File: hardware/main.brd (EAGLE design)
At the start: 91.5 x 58.5 mm, 40 parts, among them U1 TMS320F28069_PN_80, U10 TXB0101_DBV_6, U2 TXB0101_DBV_6, U3 TS3A5018_PW_16, U4 TS3A5018_PW_16, U5 SN74LVC4245A_DW_24, U7 Value, U8 Value, U9 SN74LVC4245A_DW_24

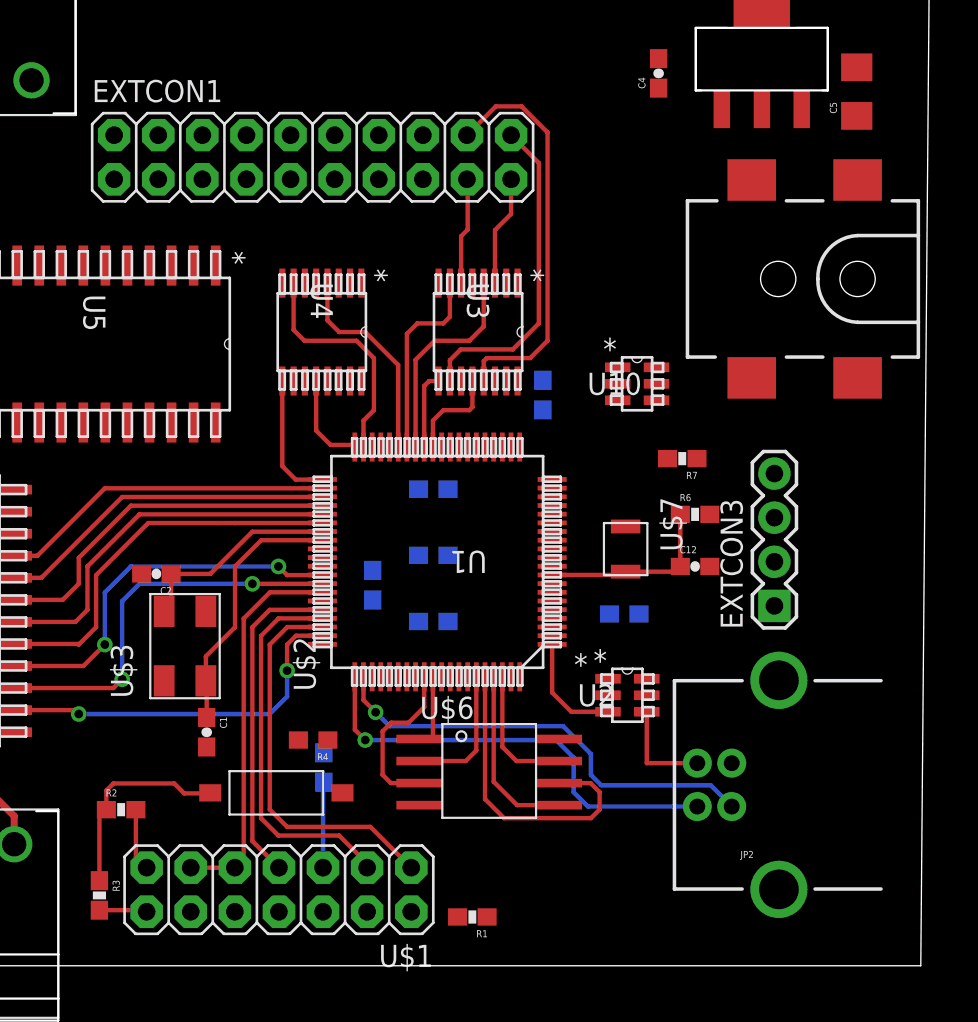
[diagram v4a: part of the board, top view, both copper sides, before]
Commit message: Ripped up USB routing, SPI routing, and previously made input stage routing. Starting over.
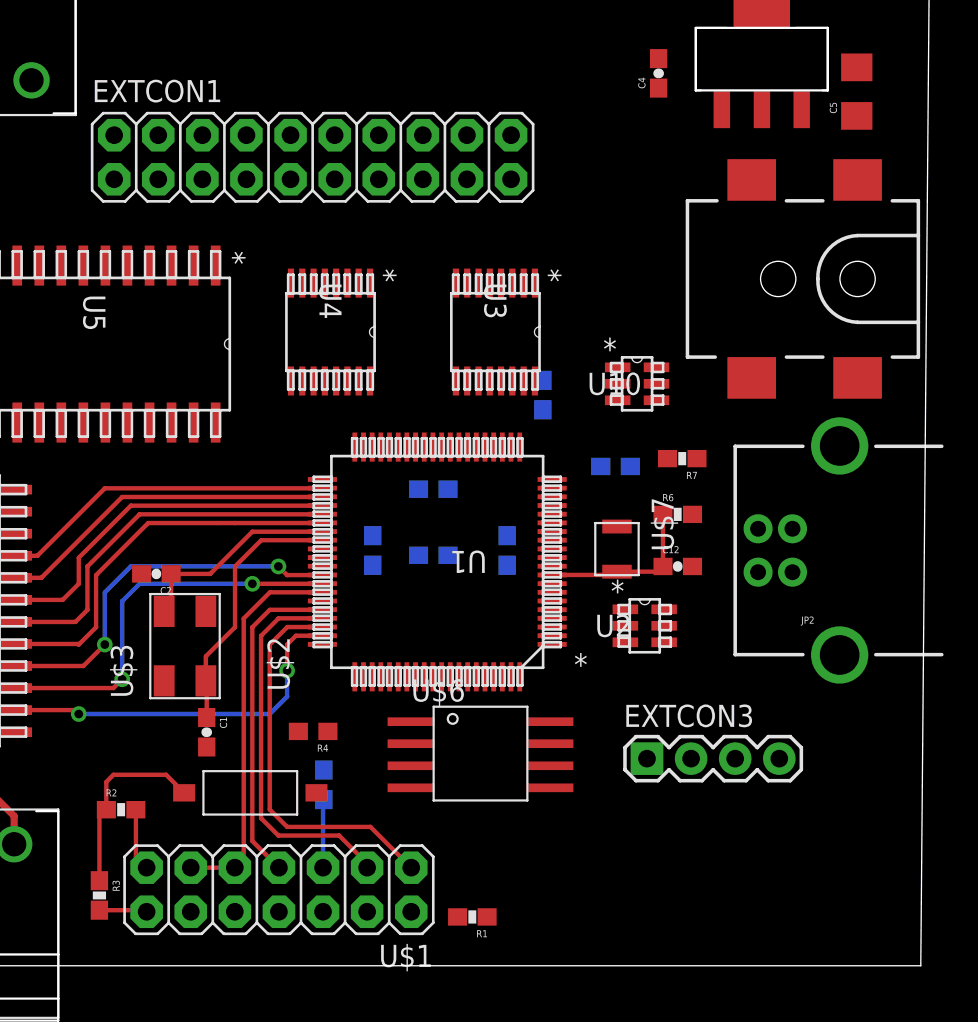
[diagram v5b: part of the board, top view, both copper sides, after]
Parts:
- moved JP2 13.9 mm to (83.6, 23.9)
- moved EXTCON3 11.5 mm to (75.2, 11.9), turned to 0 degrees
- moved C8 8.51 mm to (73.4, 28.8)
- moved C11 5.90 mm to (67.2, 23.9), turned to 270 degrees
- moved U2 4.12 mm to (75.1, 19.6)
- moved C7 2.00 mm to (59.4, 23.9)
- moved U$2 1.50 mm to (52.4, 9.96)
- moved U$6 1.12 mm to (65.6, 12.2)
- moved C12 1.00 mm to (77.0, 23.0)
- moved C6 1.00 mm to (56.6, 10.4)
- moved R6 1.00 mm to (77.0, 26.0)
- moved U3 1.00 mm to (66.5, 36.5)
- moved R4 0.50 mm to (56.0, 13.5)
- moved U$7 0.50 mm to (73.5, 24.0)
- moved U4 0.50 mm to (57.0, 36.5)
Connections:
- net USBDM renamed USB_N
- net USBDP renamed USB_P
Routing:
- net USB_P: track 25.8 -> 0.00 mm, vias 1 -> 0
- net USB_N: track 25.8 -> 0.00 mm, vias 1 -> 0
- net SW4: track 23.3 -> 0.00 mm
- net SW3: track 18.7 -> 0.00 mm
- net SPICLK: track 17.9 -> 0.00 mm
- net UCIN6: track 13.4 -> 0.00 mm
- net UCIN1: track 12.2 -> 0.00 mm
- net UCIN5: track 12.0 -> 0.00 mm
- net UCIN2: track 11.3 -> 0.00 mm
- net SPISIMO: track 10.3 -> 0.00 mm
- net !FLASHWP!: track 9.56 -> 0.00 mm
- net SPISOMI: track 7.76 -> 0.00 mm
- net !FLASHHOLD!: track 7.62 -> 0.00 mm
- net UCIN7: track 7.54 -> 0.00 mm
- net USBMON: track 6.63 -> 0.00 mm
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
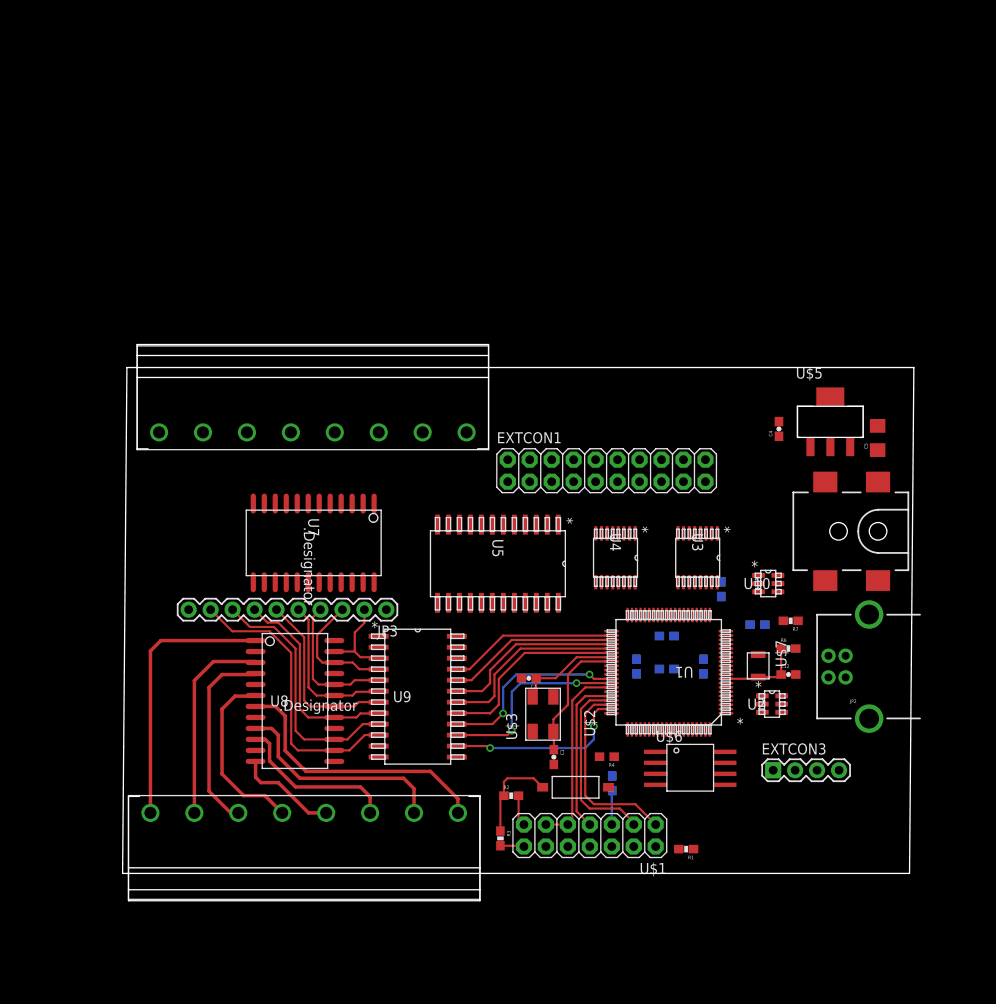
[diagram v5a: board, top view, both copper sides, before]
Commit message: Beginning new layout and routing. Clock traces and USB routed first.
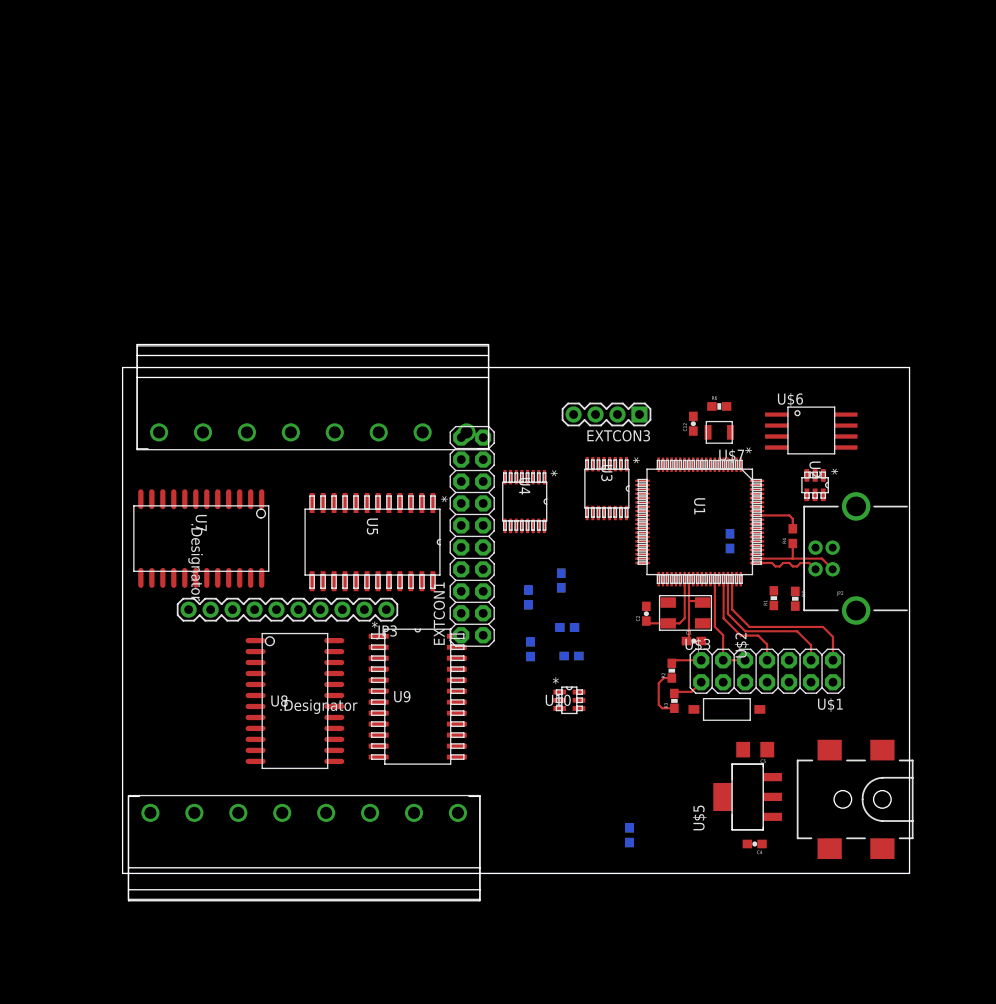
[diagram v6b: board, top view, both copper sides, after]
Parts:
- moved C4 48.1 mm to (73.1, 3.40), turned to 180 degrees
- moved U$5 44.4 mm to (72.3, 8.84), turned to 90 degrees
- moved EXTCON3 43.9 mm to (59.8, 53.1), turned to 180 degrees
- moved U$6 41.4 mm to (79.6, 51.2)
- moved C5 38.7 mm to (73.2, 14.3), turned to 180 degrees
- moved R4 33.4 mm to (77.5, 39.0), turned to 90 degrees
- moved C12 31.0 mm to (66.0, 52.0), turned to 90 degrees
- moved JP1 31.0 mm to (87.9, 8.56)
- moved R1 30.7 mm to (75.3, 31.8), turned to 90 degrees
- moved R6 29.1 mm to (69.0, 54.0)
- moved U$1 28.0 mm to (82.2, 24.6)
- moved U$7 27.4 mm to (69.0, 51.0), turned to 180 degrees
- moved U10 26.7 mm to (51.7, 20.0)
- moved U2 25.8 mm to (80.1, 44.9), turned to 270 degrees
- moved R3 25.6 mm to (63.8, 19.9), turned to 90 degrees
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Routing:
- net N$9: track 33.1 -> 0.00 mm
- net N$20: track 31.8 -> 0.00 mm
- net N$13: track 31.4 -> 0.00 mm
- net N$10: track 29.4 -> 0.00 mm
- net N$19: track 25.5 -> 0.00 mm
- net N$11: track 24.1 -> 0.00 mm
- net N$14: track 23.4 -> 0.00 mm
- net UCOUT7: track 23.0 -> 0.00 mm, vias 2 -> 0
- net UCOUT5: track 22.6 -> 0.00 mm
- net N$15: track 22.5 -> 0.00 mm
- net UCOUT6: track 22.2 -> 0.00 mm, vias 2 -> 0
- net UCOUT4: track 21.9 -> 0.00 mm
- net UCOUT8: track 21.6 -> 0.00 mm, vias 2 -> 0
- net UCOUT3: track 21.0 -> 0.00 mm
- net N$12: track 20.9 -> 0.00 mm
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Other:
- board size 91.5 x 58.5 mm -> 91 x 58.5 mm

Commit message: Change analog switch for input selection to buffer. Reviewed and reworked enable pin logic. Added single NOT gate and 5V buffer to ControllerCard library
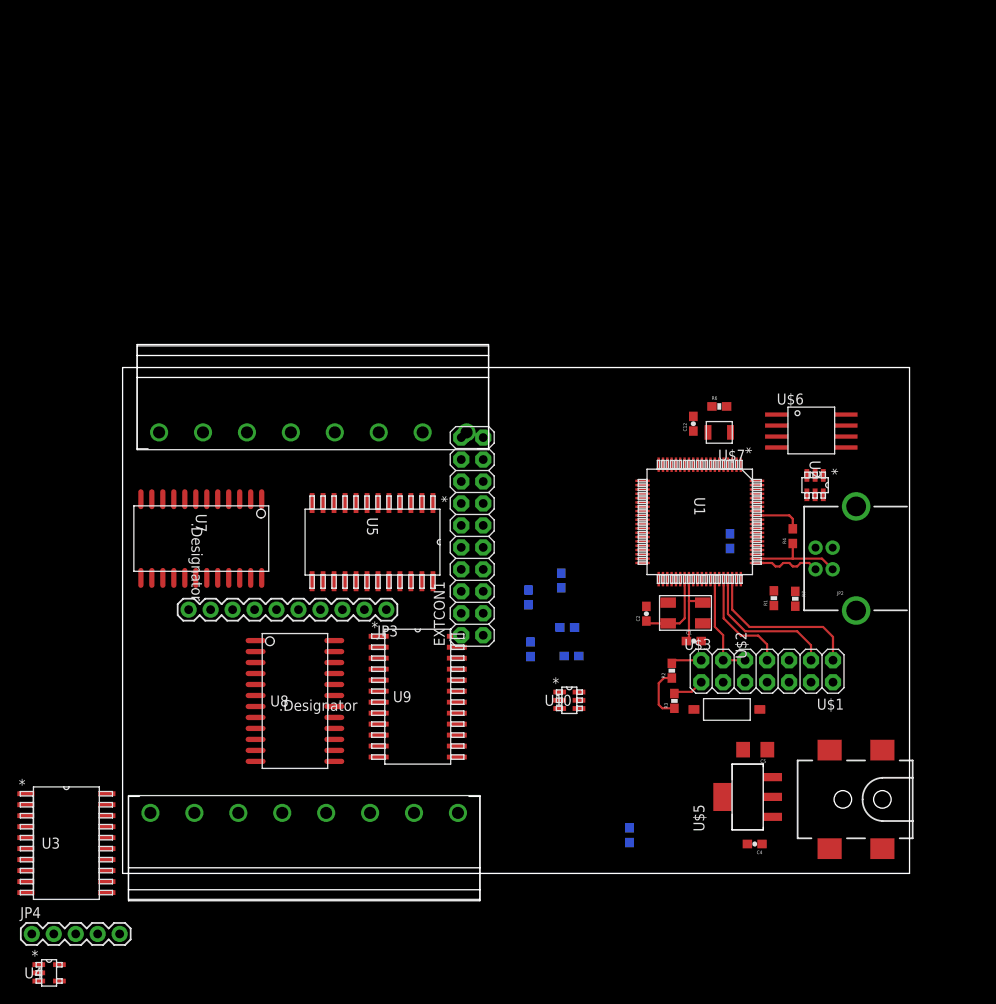
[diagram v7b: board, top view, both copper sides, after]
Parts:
- removed EXTCON3: (no value), SparkFun-Connectors:1X04
- added JP4: (no value), SparkFun-Connectors:1X05
- U3: value TS3A5018_PW_16 -> SN74ABT541B_DW_20; device ControllerCard:PW16 -> ControllerCard:DW20
- U4: value TS3A5018_PW_16 -> SN74LVC1G04_DBV_5; device ControllerCard:PW16 -> ControllerCard:DBV5
- moved U4 77.4 mm to (-8.50, -11.5), turned to 0 degrees
- moved U3 74.7 mm to (-6.50, 3.50), turned to 0 degrees
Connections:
- removed net SW1: EXTCON1.19, U3.3
- removed net SW2: EXTCON1.17, U3.6
- removed net SW3: EXTCON1.20, U3.10
- removed net SW4: EXTCON1.18, U3.13
- removed net SW5: EXTCON1.15, U4.3
- removed net SW6: EXTCON1.13, U4.6
- removed net SW7: EXTCON1.16, U4.10
- removed net SW8: EXTCON1.14, U4.13
- new net !INSEL!: U3.1, U3.19, U4.4
- new net N$29: EXTCON1.4, U3.2
- new net N$30: EXTCON1.6, U3.3
- new net N$31: EXTCON1.8, U3.4
- new net N$32: EXTCON1.10, U3.5
- new net N$33: EXTCON1.12, U3.6
- new net N$34: EXTCON1.14, U3.7
- new net N$35: EXTCON1.16, U3.8
- new net N$36: EXTCON1.18, U3.9
- net !BUFEN!: no longer U7.13, U7.24
- net !ENEXT!: no longer U3.15, U4.15
- net 3.3V: now also JP4.4; no longer EXTCON1.1, EXTCON1.11, EXTCON3.4, U3.16, U4.16
- net 5V: now also EXTCON1.1, EXTCON1.19, JP4.5, U3.20, U4.5
- net BIN1: no longer U3.2
- net BIN2: no longer U3.5
- net BIN3: no longer U3.11
- net BIN4: no longer U3.14
- net BIN5: no longer U4.2
- net BIN6: no longer U4.5
- net BIN7: no longer U4.11
- net BIN8: no longer U4.14
- net GND: now also EXTCON1.20, JP4.1, U3.10, U4.3; no longer EXTCON1.12, EXTCON3.1, U3.8, U4.8
- net IBUFOUT1: now also EXTCON1.3, U3.18; no longer EXTCON1.9
- net IBUFOUT2: now also EXTCON1.5, U3.17; no longer EXTCON1.7
- net IBUFOUT3: now also EXTCON1.7, U3.16; no longer EXTCON1.5
- net IBUFOUT4: now also EXTCON1.9, U3.15; no longer EXTCON1.3
- net IBUFOUT5: now also EXTCON1.11, U3.14; no longer EXTCON1.10
- net IBUFOUT6: now also EXTCON1.13, U3.13; no longer EXTCON1.8
- net IBUFOUT7: now also EXTCON1.15, U3.12; no longer EXTCON1.6
- net IBUFOUT8: now also EXTCON1.17, U3.11; no longer EXTCON1.4
- net INSEL: now also JP4.3, U4.2, U7.13, U7.24; no longer EXTCON3.3, U3.1, U4.1
- net RUNSEL: now also JP4.2; no longer EXTCON3.2
- net UCIN1: no longer U3.4
- net UCIN2: no longer U3.7
- net UCIN3: no longer U3.9
- net UCIN4: no longer U3.12
- net UCIN5: no longer U4.4
- net UCIN6: no longer U4.7
- net UCIN7: no longer U4.9
- net UCIN8: no longer U4.12

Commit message: Finished routing part of the board. Rearranged input connector in schematic.
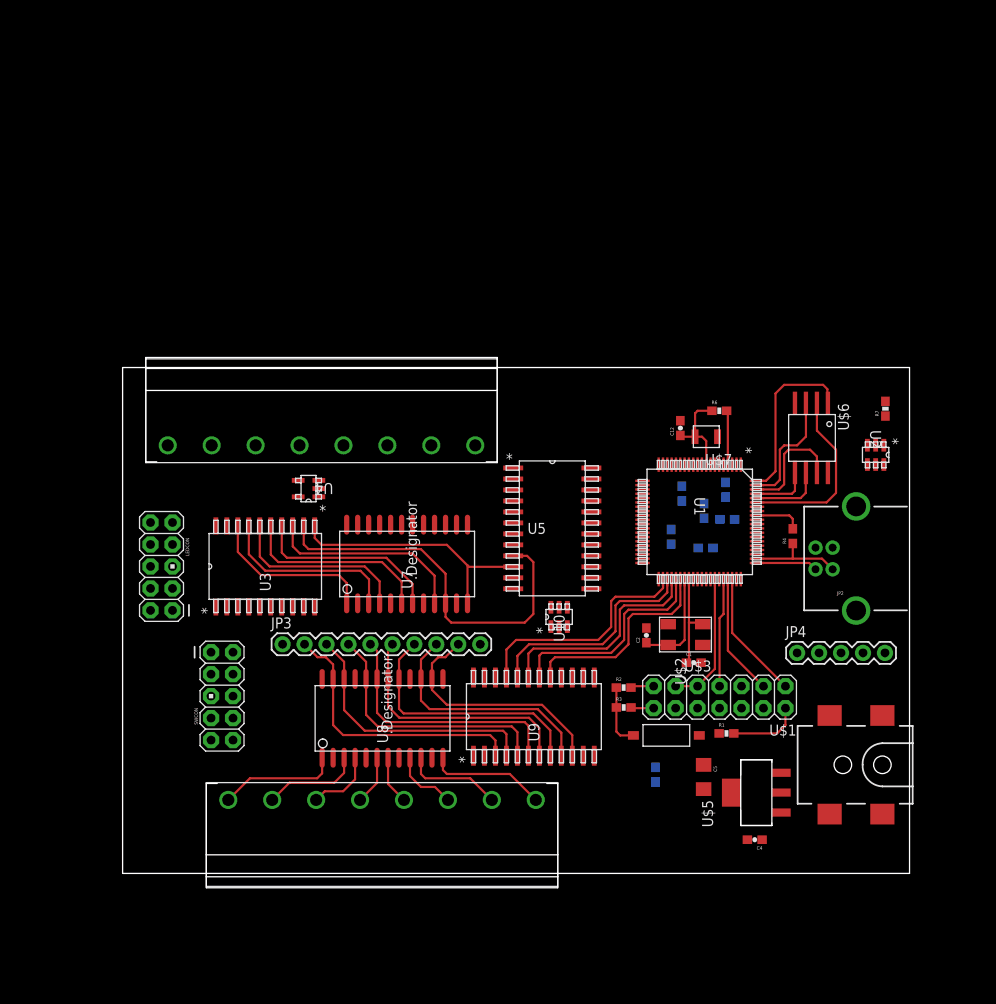
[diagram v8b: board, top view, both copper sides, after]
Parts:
- removed EXTCON1: M10X2, SparkFun-Connectors:2X10
- added LEDCON, SWCON: M05X2PTH, SparkFun-Connectors:AVR_ICSP
- moved JP4 94.3 mm to (78.0, 25.5)
- moved U4 63.5 mm to (21.5, 44.5), turned to 180 degrees
- moved U3 39.4 mm to (16.5, 35.5), turned to 90 degrees
- moved C11 25.1 mm to (64.7, 43.9)
- moved R7 24.3 mm to (88.2, 53.7), turned to 90 degrees
- moved U7 24.0 mm to (32.9, 35.8), turned to 90 degrees
- moved C9 22.3 mm to (69.9, 41.0)
- moved R5 21.7 mm to (69.7, 44.4)
- moved U5 20.9 mm to (49.7, 39.9), turned to 0 degrees
- moved C10 19.9 mm to (67.4, 37.6)
- moved C7 17.9 mm to (63.4, 38.9)
- moved R1 16.6 mm to (69.8, 16.2), turned to 0 degrees
- moved U9 13.6 mm to (47.6, 18.1), turned to 90 degrees
- moved JP3 12.6 mm to (18.5, 26.5), turned to 0 degrees
- moved U8 10.3 mm to (30.1, 17.9), turned to 90 degrees
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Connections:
- removed net BIN1: U5.21
- removed net BIN2: U5.20
- removed net BIN3: U5.19
- removed net BIN4: U5.18
- removed net BIN5: U5.17
- removed net BIN6: U5.16
- removed net BIN7: U5.15
- removed net BIN8: U5.14
- new net N$37: SWCON.8, U3.9
- net !FLASHEN!: now also U1.80; no longer U1.70
- net !FLASHWP!: now also U1.79; no longer U1.69
- net 5V: now also LEDCON.9, SWCON.9; no longer EXTCON1.1, EXTCON1.19
- net GND: now also LEDCON.10; no longer EXTCON1.2, EXTCON1.20
- net IBUFOUT1: now also LEDCON.1; no longer EXTCON1.3
- net IBUFOUT2: now also LEDCON.3; no longer EXTCON1.5
- net IBUFOUT3: now also LEDCON.5; no longer EXTCON1.7
- net IBUFOUT4: now also LEDCON.7; no longer EXTCON1.9
- net IBUFOUT5: now also LEDCON.2; no longer EXTCON1.11
- net IBUFOUT6: now also LEDCON.4; no longer EXTCON1.13
- net IBUFOUT7: now also LEDCON.6; no longer EXTCON1.15
- net IBUFOUT8: now also LEDCON.8; no longer EXTCON1.17
- net N$17: now also U$4.P$8; no longer U$4.P$5
- net N$18: now also U$4.P$7; no longer U$4.P$6
- net N$19: now also U$4.P$6; no longer U$4.P$7
- net N$20: now also U$4.P$5; no longer U$4.P$8
- net N$21: now also U$8.P$8; no longer U$8.P$1
- net N$22: now also U$8.P$7; no longer U$8.P$2
- net N$23: now also U$8.P$6; no longer U$8.P$3
- net N$24: now also U$8.P$5; no longer U$8.P$4
- net N$25: now also U$8.P$1; no longer U$8.P$8
- net N$26: now also U$8.P$2; no longer U$8.P$7
- net N$27: now also U$8.P$3; no longer U$8.P$6
- net N$28: now also U$8.P$4; no longer U$8.P$5
- net N$29: now also SWCON.1; no longer EXTCON1.4
- net N$30: now also SWCON.3; no longer EXTCON1.6
- net N$31: now also SWCON.5; no longer EXTCON1.8
- net N$32: now also SWCON.7; no longer EXTCON1.10
- net N$33: now also SWCON.2; no longer EXTCON1.12
- net N$34: now also SWCON.4; no longer EXTCON1.14
- net N$35: now also SWCON.6; no longer EXTCON1.16
- net N$36: now also SWCON.10; no longer EXTCON1.18, U3.9
- net UCIN1: now also U1.31, U5.21; no longer U1.33
- net UCIN2: now also U1.32, U5.20; no longer U1.34
- net UCIN3: now also U1.33, U5.19; no longer U1.32
- net UCIN4: now also U1.34, U5.18; no longer U1.31
- net UCIN5: now also U5.17
- net UCIN6: now also U5.16
- net UCIN7: now also U1.40, U5.15; no longer U1.41
- net UCIN8: now also U1.41, U5.14; no longer U1.40
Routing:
- net IBUFOUT7: track 0.00 -> 44.4 mm
- net N$5: track 0.00 -> 32.6 mm
- net N$6: track 0.00 -> 30.9 mm
- net IBUFOUT8: track 0.00 -> 30.1 mm
- net N$7: track 0.00 -> 30.1 mm
- net N$8: track 0.00 -> 29.8 mm
- net N$11: track 0.00 -> 29.7 mm
- net N$12: track 0.00 -> 29.1 mm
- net N$9: track 0.00 -> 27.8 mm
- net N$10: track 0.00 -> 27.7 mm
- net UCOUT1: track 0.00 -> 27.1 mm
- net UCOUT2: track 0.00 -> 26.2 mm
- net UCOUT3: track 0.00 -> 25.9 mm
- net UCOUT4: track 0.00 -> 25.3 mm
- net UCOUT5: track 0.00 -> 24.3 mm
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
